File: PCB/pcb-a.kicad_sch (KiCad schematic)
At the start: 16 parts, among them Q3 BC337, Q4 BC337, SW1 config, U1 MCP23008-xP, U4 ATmega16L-8P

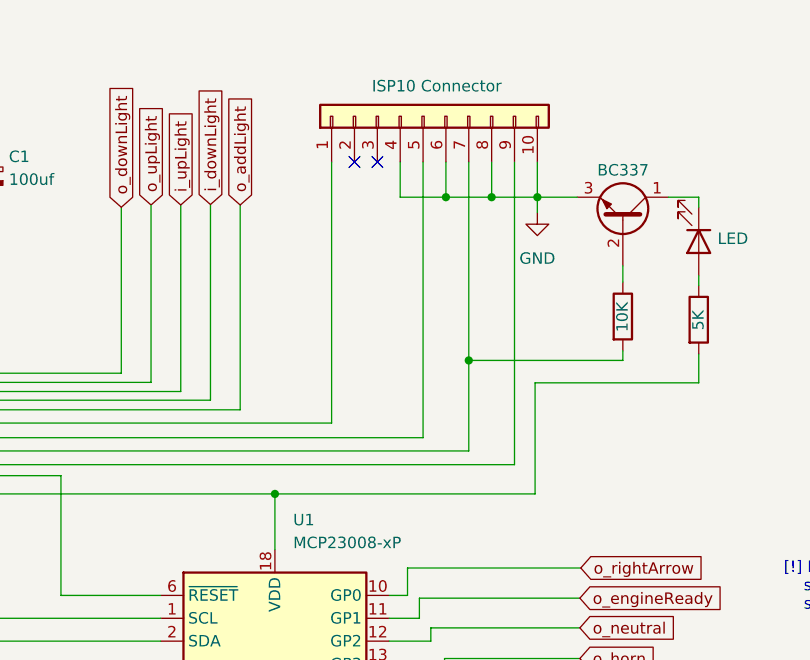
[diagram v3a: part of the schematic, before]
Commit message: Fix for (USB-ASP compliant) ISP-10pin connector
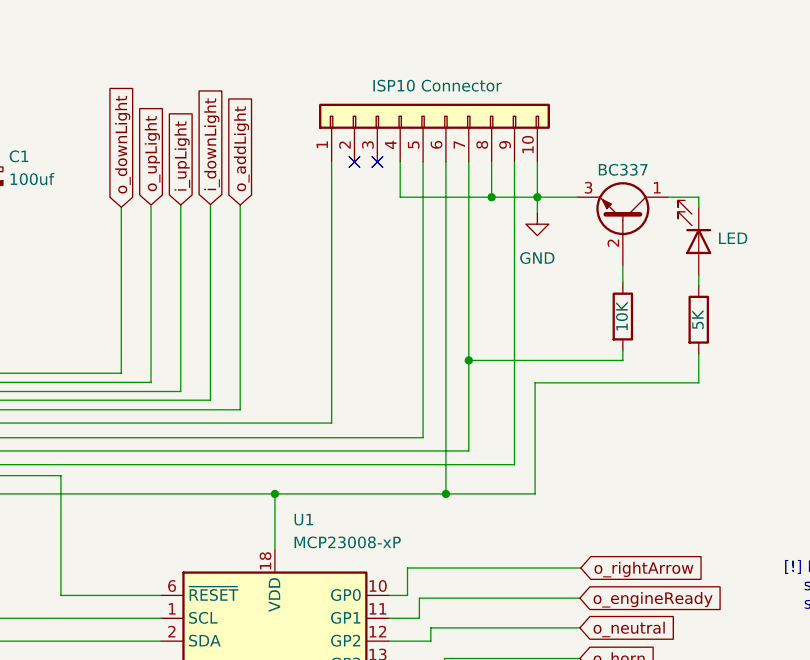
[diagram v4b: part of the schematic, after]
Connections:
- net GND: no longer ISP101.6 (Pin_6)
- net tempPower: now also ISP101.6 (Pin_6)
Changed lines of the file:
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@@
   (junction (at 49.53 168.5544) (diameter 0) (color 0 0 0 0)
   )
+  (junction (at 186.9948 86.3092) (diameter 0) (color 0 0 0 0)
+  )
   (junction (at 123.0884 59.1312) (diameter 0) (color 0 0 0 0)
   )
@@
   )
   (junction (at 129.5908 43.6372) (diameter 0) (color 0 0 0 0)
-  )
-  (junction (at 186.9948 53.34) (diameter 0) (color 0 0 0 0)
   )
   (junction (at 76.8604 143.5608) (diameter 0) (color 0 0 0 0)
@@
     (stroke (width 0) (type default) (color 0 0 0 0))
   )
+  (wire (pts (xy 186.9948 86.3092) (xy 196.9008 86.3092))
+    (stroke (width 0) (type default) (color 0 0 0 0))
+  )
   (wire (pts (xy 74.3204 118.618) (xy 86.868 118.618))
     (stroke (width 0) (type default) (color 0 0 0 0))
@@
     (stroke (width 0) (type default) (color 0 0 0 0))
   )
-  (wire (pts (xy 186.9948 53.34) (xy 186.9948 49.4284))
-    (stroke (width 0) (type default) (color 0 0 0 0))
-  )
   (wire (pts (xy 132.842 139.0396) (xy 86.868 139.0396))
     (stroke (width 0) (type default) (color 0 0 0 0))
@@
     (stroke (width 0) (type default) (color 0 0 0 0))
   )
-  (wire (pts (xy 192.0748 53.34) (xy 186.9948 53.34))
+  (wire (pts (xy 181.9148 53.34) (xy 192.0748 53.34))
     (stroke (width 0) (type default) (color 0 0 0 0))
   )
@@
     (stroke (width 0) (type default) (color 0 0 0 0))
   )
-  (wire (pts (xy 186.9948 53.34) (xy 181.9148 53.34))
-    (stroke (width 0) (type default) (color 0 0 0 0))
-  )
   (wire (pts (xy 106.3752 136.2456) (xy 89.8144 136.2456))
     (stroke (width 0) (type default) (color 0 0 0 0))
@@
     (stroke (width 0) (type default) (color 0 0 0 0))
   )
+  (wire (pts (xy 186.9948 49.4284) (xy 186.9948 86.3092))
+    (stroke (width 0) (type default) (color 0 0 0 0))
+  )
   (wire (pts (xy 152.4 117.9068) (xy 155.2956 117.9068))
     (stroke (width 0) (type default) (color 0 0 0 0))
@@
     (stroke (width 0) (type default) (color 0 0 0 0))
   )
-  (wire (pts (xy 167.9956 86.3092) (xy 196.9008 86.3092))
-    (stroke (width 0) (type default) (color 0 0 0 0))
-  )
+  (wire (pts (xy 167.9956 86.3092) (xy 186.9948 86.3092))
+    (stroke (width 0) (type default) (color 0 0 0 0))
+  )

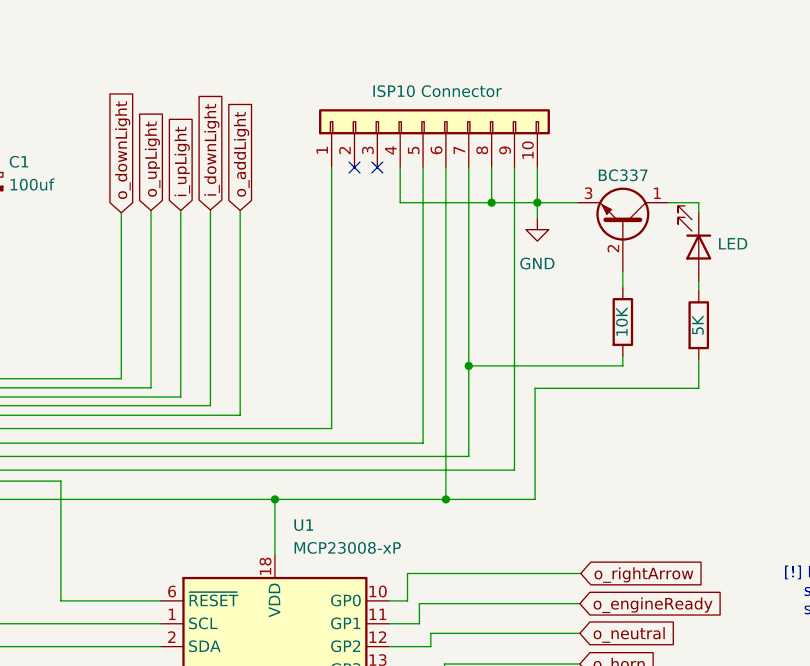
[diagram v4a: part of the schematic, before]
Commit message: Wrong position for VTAG pin fixed
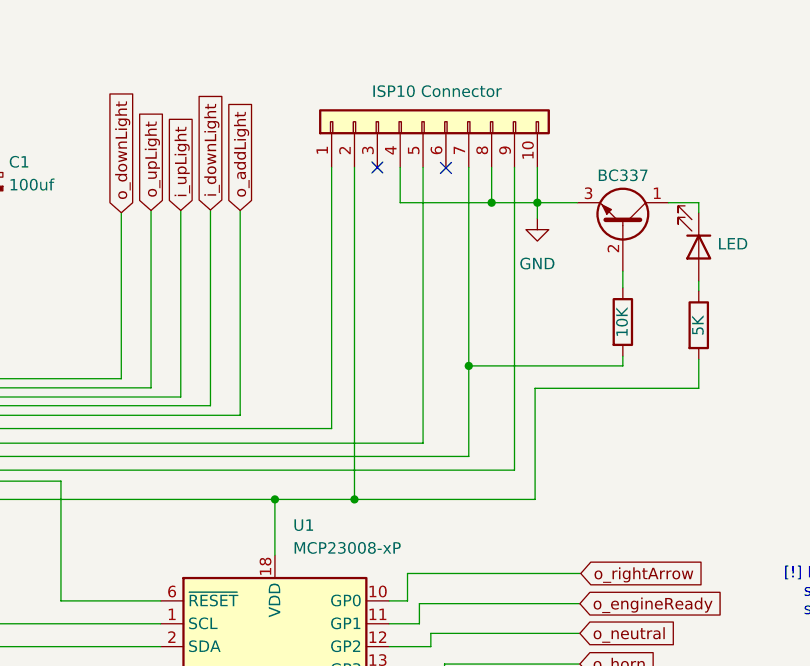
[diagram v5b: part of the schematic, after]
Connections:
- net tempPower: now also ISP101.2 (Pin_2); no longer ISP101.6 (Pin_6)
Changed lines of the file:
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@@
   (junction (at 49.53 168.5544) (diameter 0) (color 0 0 0 0)
   )
-  (junction (at 186.9948 86.3092) (diameter 0) (color 0 0 0 0)
-  )
   (junction (at 123.0884 59.1312) (diameter 0) (color 0 0 0 0)
   )
@@
   )
   (junction (at 197.1548 53.34) (diameter 0) (color 0 0 0 0)
+  )
+  (junction (at 176.8348 86.3092) (diameter 0) (color 0 0 0 0)
   )
   (junction (at 152.4 115.3668) (diameter 0) (color 0 0 0 0)
@@
   (no_connect (at 179.3748 49.4284))
   (no_connect (at 74.3204 62.738))
-  (no_connect (at 176.8348 49.4284))
+  (no_connect (at 186.9948 49.4792))
   (no_connect (at 61.6204 42.418))
   (no_connect (at 74.3204 60.198))
@@
     (stroke (width 0) (type default) (color 0 0 0 0))
   )
-  (wire (pts (xy 186.9948 86.3092) (xy 196.9008 86.3092))
+  (wire (pts (xy 167.9956 86.3092) (xy 176.8348 86.3092))
     (stroke (width 0) (type default) (color 0 0 0 0))
   )
@@
     (stroke (width 0) (type default) (color 0 0 0 0))
   )
-  (wire (pts (xy 186.9948 49.4284) (xy 186.9948 86.3092))
-    (stroke (width 0) (type default) (color 0 0 0 0))
-  )
   (wire (pts (xy 152.4 117.9068) (xy 155.2956 117.9068))
     (stroke (width 0) (type default) (color 0 0 0 0))
@@
     (stroke (width 0) (type default) (color 0 0 0 0))
   )
+  (wire (pts (xy 176.8348 86.3092) (xy 196.9008 86.3092))
+    (stroke (width 0) (type default) (color 0 0 0 0))
+  )
   (wire (pts (xy 80.8228 78.4352) (xy 174.2948 78.4352))
     (stroke (width 0) (type default) (color 0 0 0 0))
@@
     (stroke (width 0) (type default) (color 0 0 0 0))
   )
+  (wire (pts (xy 176.8348 49.4284) (xy 176.8348 86.3092))
+    (stroke (width 0) (type default) (color 0 0 0 0))
+  )
   (wire (pts (xy 182.8292 118.7704) (xy 202.1332 118.7704))
     (stroke (width 0) (type default) (color 0 0 0 0))
@@
     (stroke (width 0) (type default) (color 0 0 0 0))
   )
-  (wire (pts (xy 167.9956 86.3092) (xy 186.9948 86.3092))
-    (stroke (width 0) (type default) (color 0 0 0 0))
-  )
